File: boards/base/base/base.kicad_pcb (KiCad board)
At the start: 2 copper layers, 70.9 x 71 mm, 26 parts, among them J1 Conn_01x04_Female, J2 Conn_01x06_Female, J3 Conn_01x06_Female, J4 Screw_Terminal_01x02, J5 Conn_01x03_Female, J6 Conn_01x02_Male, Q1 BC547, Q2 BC547, Q3 2SD1047, Q4 BCP56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

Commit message: Final version of BasePCB
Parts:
- removed R6: 220, Resistor_SMD:R_0805_2012Metric
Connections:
- J5 pad 2: Net-(J5-Pad2) -> Din
- U2 pad 27: CAB_EN -> unconnected-(U2-Pad27)
- U2 pad 28: Din -> unconnected-(U2-Pad28)
- U2 pad 29: unconnected-(U2-Pad29) -> CAB_EN
- U2 pad 30: unconnected-(U2-Pad30) -> Din
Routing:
- net Din: track 5.78 -> 46.5 mm
- net Net-(J5-Pad2): track 34.7 -> 0.00 mm
- net CAB_EN: track 56.6 -> 58.0 mm
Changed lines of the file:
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@@
   (net 28 "/CAB_GROUND")
   (net 29 "Net-(Q4-Pad1)")
-  (net 30 "unconnected-(U2-Pad29)")
-  (net 31 "unconnected-(U2-Pad30)")
+  (net 30 "unconnected-(U2-Pad27)")
+  (net 31 "unconnected-(U2-Pad28)")
   (net 32 "unconnected-(U2-Pad31)")
   (net 33 "SDA")
@@
   (net 51 "CAB_RESET")
   (net 52 "Din")
-  (net 53 "Net-(J5-Pad2)")
   (footprint "TerminalBlock:TerminalBlock_Altech_AK300-2_P5.00mm" (layer "F.Cu")
     (at 115.8 93 -90)
@@
     )
   )
-  (footprint "Resistor_SMD:R_0805_2012Metric" (layer "F.Cu")
-    (at 102.7 102.9875 -90)
-    (descr "Resistor SMD 0805 (2012 Metric), square (rectangular) end terminal, IPC_7351 nominal, (Body size source: IPC-SM-782 page 72, https://www.pcb-3d.com/wordpress/wp-content/uploads/ipc-sm-782a_amendment_1_and_2.pdf), generated with kicad-footprint-generator")
-    (tags "resistor")
-    (property "Sheetfile" "base.kicad_sch")
-    (property "Sheetname" "")
-    (attr smd)
-    (fp_text reference "R6" (at 0 -1.65 90) (layer "F.SilkS")
-      (effects (font (size 1 1) (thickness 0.15)))
-    )
-    (fp_text value "220" (at 0 1.65 90) (layer "F.Fab")
-      (effects (font (size 1 1) (thickness 0.15)))
-    )
-    (fp_text user "${REFERENCE}" (at 0 0 90) (layer "F.Fab")
-      (effects (font (size 0.5 0.5) (thickness 0.08)))
-    )
-    (fp_line (start -0.227064 0.735) (end 0.227064 0.735) (layer "F.SilkS") (width 0.12))
-    (fp_line (start -0.227064 -0.735) (end 0.227064 -0.735) (layer "F.SilkS") (width 0.12))
-    (fp_line (start 1.68 0.95) (end -1.68 0.95) (layer "F.CrtYd") (width 0.05))
-    (fp_line (start -1.68 0.95) (end -1.68 -0.95) (layer "F.CrtYd") (width 0.05))
-    (fp_line (start 1.68 -0.95) (end 1.68 0.95) (layer "F.CrtYd") (width 0.05))
-    (fp_line (start -1.68 -0.95) (end 1.68 -0.95) (layer "F.CrtYd") (width 0.05))
-    (fp_line (start 1 0.625) (end -1 0.625) (layer "F.Fab") (width 0.1))
-    (fp_line (start 1 -0.625) (end 1 0.625) (layer "F.Fab") (width 0.1))
-    (fp_line (start -1 -0.625) (end 1 -0.625) (layer "F.Fab") (width 0.1))
-    (fp_line (start -1 0.625) (end -1 -0.625) (layer "F.Fab") (width 0.1))
-    (pad "1" smd roundrect (at -0.9125 0 270) (size 1.025 1.4) (layers "F.Cu" "F.Paste" "F.Mask") (roundrect_rratio 0.243902439)
-      (net 53 "Net-(J5-Pad2)") (pintype "passive"))
-    (pad "2" smd roundrect (at 0.9125 0 270) (size 1.025 1.4) (layers "F.Cu" "F.Paste" "F.Mask") (roundrect_rratio 0.243902439)
-      (net 52 "Din") (pintype "passive"))
-    (model "${KICAD6_3DMODEL_DIR}/Resistor_SMD.3dshapes/R_0805_2012Metric.wrl"
-      (offset (xyz 0 0 0))
-      (scale (xyz 1 1 1))
-      (rotate (xyz 0 0 0))
-    )
-  )
   (footprint "StackCabinet:XLE1509" (layer "F.Cu")
     (at 119.253 64.516)
@@
       (net 2 "GND") (pinfunction "Pin_1") (pintype "passive"))
     (pad "2" thru_hole oval (at 0 2.54 270) (size 1.7 1.7) (drill 1) (layers *.Cu *.Mask)
-      (net 53 "Net-(J5-Pad2)") (pinfunction "Pin_2") (pintype "passive"))
+      (net 52 "Din") (pinfunction "Pin_2") (pintype "passive"))
     (pad "3" thru_hole oval (at 0 5.08 270) (size 1.7 1.7) (drill 1) (layers *.Cu *.Mask)
       (net 3 "5V") (pinfunction "Pin_3") (pintype "passive"))
@@
     (fp_arc (start -1.91 -1.91) (mid 0 -2.701148) (end 1.91 -1.91) (layer "F.Fab") (width 0.1))
     (fp_arc (start 1.91 1.91) (mid 0 2.701148) (end -1.91 1.91) (layer "F.Fab") (width 0.1))
-    (pad "1" smd rect (at -2.75 0 180) (size 1.5 2.4) (layers "F.Cu" "F.Paste" "F.Mask")
+    (pad "1" smd rect (at -3.2 0 180) (size 2.4 2.4) (layers "F.Cu" "F.Paste" "F.Mask")
       (net 4 "Net-(D1-Pad1)") (pinfunction "1") (pintype "passive"))
-    (pad "2" smd rect (at 2.75 0 180) (size 1.5 2.4) (layers "F.Cu" "F.Paste" "F.Mask")
+    (pad "2" smd rect (at 3.2 0 180) (size 2.4 2.4) (layers "F.Cu" "F.Paste" "F.Mask")
       (net 3 "5V") (pinfunction "2") (pintype "passive"))
     (model "${KICAD6_3DMODEL_DIR}/Inductor_SMD.3dshapes/L_6.3x6.3_H3.wrl"
@@
       (net 27 "unconnected-(U2-Pad26)") (pinfunction "GPIO20/USB_D+") (pintype "bidirectional"))
     (pad "27" thru_hole oval (at 22.75 -27.94) (size 1.2 2) (drill 0.8) (layers *.Cu *.Mask)
-      (net 50 "CAB_EN") (pinfunction "GPIO21") (pintype "bidirectional"))
+      (net 30 "unconnected-(U2-Pad27)") (pinfunction "GPIO21") (pintype "bidirectional"))
     (pad "28" thru_hole oval (at 22.75 -25.4) (size 1.2 2) (drill 0.8) (layers *.Cu *.Mask)
-      (net 52 "Din") (pinfunction "GPIO47") (pintype "bidirectional"))
+      (net 31 "unconnected-(U2-Pad28)") (pinfunction "GPIO47") (pintype "bidirectional"))
     (pad "29" thru_hole oval (at 22.75 -22.86) (size 1.2 2) (drill 0.8) (layers *.Cu *.Mask)
-      (net 30 "unconnected-(U2-Pad29)") (pinfunction "GPIO48") (pintype "bidirectional"))
+      (net 50 "CAB_EN") (pinfunction "GPIO48") (pintype "bidirectional"))
     (pad "30" thru_hole oval (at 22.75 -20.32) (size 1.2 2) (drill 0.8) (layers *.Cu *.Mask)
-      (net 31 "unconnected-(U2-Pad30)") (pinfunction "GPIO45") (pintype "bidirectional"))
+      (net 52 "Din") (pinfunction "GPIO45") (pintype "bidirectional"))
     (pad "31" thru_hole oval (at 22.75 -17.78) (size 1.2 2) (drill 0.8) (layers *.Cu *.Mask)
       (net 32 "unconnected-(U2-Pad31)") (pinfunction "GPIO0") (pintype "bidirectional"))
@@
   (segment (start 88.646 58.674) (end 89.916 57.404) (width 0.5) (layer "F.Cu") (net 38))
   (segment (start 91.24 49.73) (end 101.28 49.73) (width 0.5) (layer "F.Cu") (net 38))
-  (segment (start 105.17656 106.02444) (end 105.17656 109.652) (width 0.5) (layer "F.Cu") (net 50))
-  (segment (start 131.572 103.124) (end 108.077 103.124) (width 0.5) (layer "F.Cu") (net 50))
-  (segment (start 138.176 80.518) (end 138.176 96.52) (width 0.5) (layer "F.Cu") (net 50))
-  (segment (start 108.077 103.124) (end 105.17656 106.02444) (width 0.5) (layer "F.Cu") (net 50))
-  (segment (start 138.176 96.52) (end 131.572 103.124) (width 0.5) (layer "F.Cu") (net 50))
+  (segment (start 124.0536 104.7496) (end 102.2096 104.7496) (width 0.5) (layer "F.Cu") (net 50))
+  (segment (start 138.176 90.6272) (end 124.0536 104.7496) (width 0.5) (layer "F.Cu") (net 50))
+  (segment (start 100.25656 106.70264) (end 100.25656 110.05) (width 0.5) (layer "F.Cu") (net 50))
+  (segment (start 102.2096 104.7496) (end 100.25656 106.70264) (width 0.5) (layer "F.Cu") (net 50))
+  (segment (start 138.176 80.518) (end 138.176 90.6272) (width 0.5) (layer "F.Cu") (net 50))
   (segment (start 85.598 76.708) (end 85.598 80.2405) (width 0.5) (layer "F.Cu") (net 51))
-  (segment (start 102.7 103.9) (end 102.63656 103.96344) (width 0.5) (layer "F.Cu") (net 52))
-  (segment (start 102.63656 103.96344) (end 102.63656 109.652) (width 0.5) (layer "F.Cu") (net 52))
-  (segment (start 129.667 93.133) (end 126.7 96.1) (width 0.5) (layer "F.Cu") (net 53))
-  (segment (start 126.7 96.1) (end 105.7 96.1) (width 0.5) (layer "F.Cu") (net 53))
-  (segment (start 105.7 96.1) (end 102.7 99.1) (width 0.5) (layer "F.Cu") (net 53))
-  (segment (start 129.667 90.805) (end 129.667 93.133) (width 0.5) (layer "F.Cu") (net 53))
-  (segment (start 102.7 99.1) (end 102.7 102.075) (width 0.5) (layer "F.Cu") (net 53))
+  (segment (start 103.9876 96.0628) (end 97.71656 102.33384) (width 0.5) (layer "F.Cu") (net 52))
+  (segment (start 129.667 94.234) (end 127.8382 96.0628) (width 0.5) (layer "F.Cu") (net 52))
+  (segment (start 129.667 90.805) (end 129.667 94.234) (width 0.5) (layer "F.Cu") (net 52))
+  (segment (start 127.8382 96.0628) (end 103.9876 96.0628) (width 0.5) (layer "F.Cu") (net 52))
+  (segment (start 97.71656 102.33384) (end 97.71656 110.05) (width 0.5) (layer "F.Cu") (net 52))
   (zone (net 2) (net_name "GND") (layer "F.Cu") (hatch edge 0.508)
     (connect_pads (clearance 0.508))

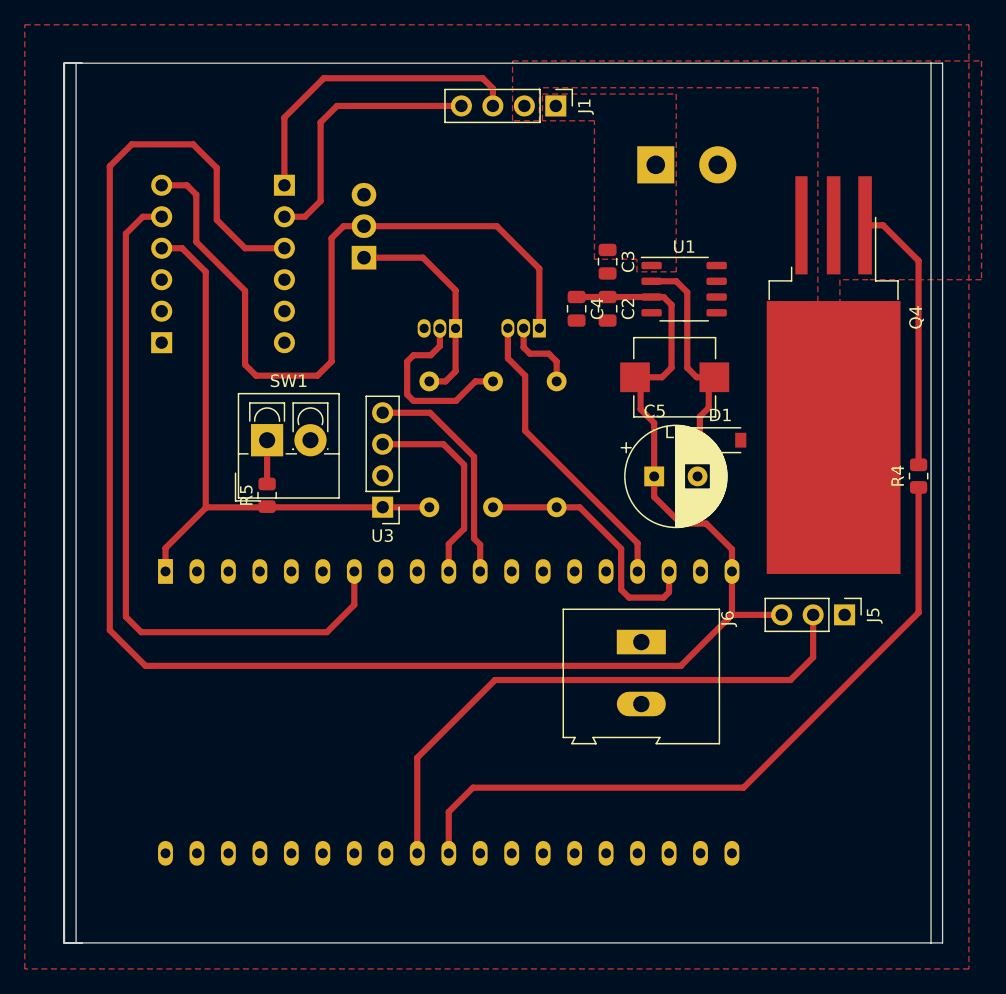
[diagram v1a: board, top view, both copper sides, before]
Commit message: Added diode on base
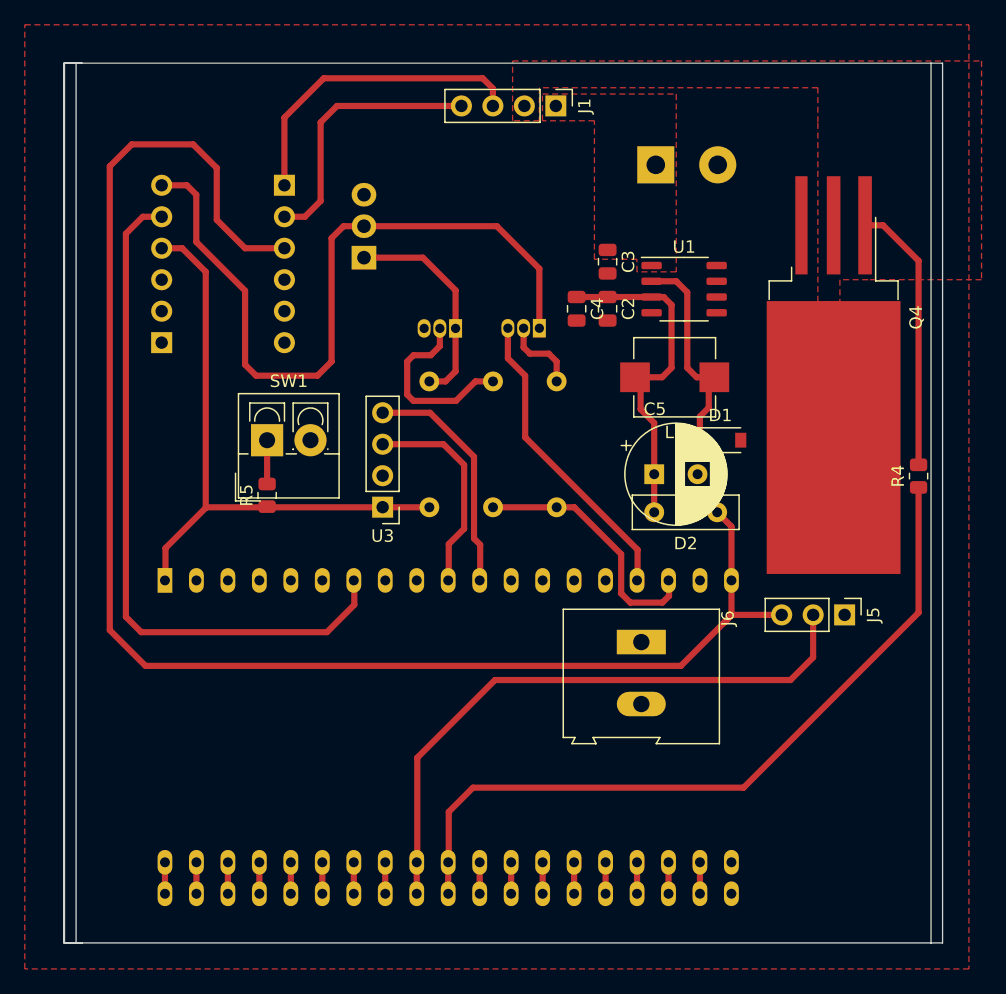
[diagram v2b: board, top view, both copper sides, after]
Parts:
- added D2: D, Resistor_THT:R_Box_L8.4mm_W2.5mm_P5.08mm, F.Cu at (121.9, 82.5)
- moved U2 0.72 mm to (77.4, 88.0)
- moved C5 0.18 mm to (116.8, 79.5)
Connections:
- C2 pad 1: 5V -> VOUT
- C4 pad 1: 5V -> VOUT
- C5 pad 1: 5V -> VOUT
- L1 pad 2: 5V -> VOUT
- U1 pad 3: 5V -> VOUT
- U2 pad 18: GND -> unconnected-(U2-Pad18)
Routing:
- net 5V: track 155.4 -> 125.0 mm
- net VOUT: track 0.00 -> 27.2 mm
- net GND: track 0.00 -> 5.08 mm
- net unconnected-(U2-Pad21): track 0.00 -> 2.54 mm
- net unconnected-(U2-Pad37): track 0.00 -> 2.54 mm
- net unconnected-(U2-Pad36): track 0.00 -> 2.54 mm
- net unconnected-(U2-Pad35): track 0.00 -> 2.54 mm
- net unconnected-(U2-Pad34): track 0.00 -> 2.54 mm
- net unconnected-(U2-Pad33): track 0.00 -> 2.54 mm
- net unconnected-(U2-Pad31): track 0.00 -> 2.54 mm
- net unconnected-(U2-Pad28): track 0.00 -> 2.54 mm
- net unconnected-(U2-Pad27): track 0.00 -> 2.54 mm
- net unconnected-(U2-Pad26): track 0.00 -> 2.54 mm
- net unconnected-(U2-Pad25): track 0.00 -> 2.54 mm
- net unconnected-(U2-Pad24): track 0.00 -> 2.54 mm
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
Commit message: Backups
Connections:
- net /CAB_GROUND renamed CAB_GROUND
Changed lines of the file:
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@@
   (net 26 "unconnected-(U2-Pad25)")
   (net 27 "unconnected-(U2-Pad26)")
-  (net 28 "/CAB_GROUND")
+  (net 28 "CAB_GROUND")
   (net 29 "Net-(Q4-Pad1)")
   (net 30 "unconnected-(U2-Pad27)")
@@
       (net 1 "VBUS") (pinfunction "Pin_1") (pintype "passive"))
     (pad "2" thru_hole oval (at 0 2.54 270) (size 1.7 1.7) (drill 1) (layers *.Cu *.Mask)
-      (net 28 "/CAB_GROUND") (pinfunction "Pin_2") (pintype "passive"))
+      (net 28 "CAB_GROUND") (pinfunction "Pin_2") (pintype "passive"))
     (pad "3" thru_hole oval (at 0 5.08 270) (size 1.7 1.7) (drill 1) (layers *.Cu *.Mask)
       (net 37 "GDA_H") (pinfunction "Pin_3") (pintype "passive"))
@@
       (net 29 "Net-(Q4-Pad1)") (pinfunction "B") (pintype "input"))
     (pad "2" smd rect (at -7.4375 0 270) (size 7.925 1.1) (layers "F.Cu" "F.Paste" "F.Mask")
-      (net 28 "/CAB_GROUND") (pinfunction "C") (pintype "passive"))
+      (net 28 "CAB_GROUND") (pinfunction "C") (pintype "passive"))
     (pad "2" smd rect (at 9.6875 0 270) (size 22.025 10.8) (layers "F.Cu" "F.Mask")
-      (net 28 "/CAB_GROUND") (pinfunction "C") (pintype "passive"))
+      (net 28 "CAB_GROUND") (pinfunction "C") (pintype "passive"))
     (pad "3" smd rect (at -7.4375 2.595 270) (size 7.925 0.99) (layers "F.Cu" "F.Paste" "F.Mask")
       (net 2 "GND") (pinfunction "E") (pintype "passive"))
@@
     )
   )
-  (zone (net 28) (net_name "/CAB_GROUND") (layer "F.Cu") (hatch edge 0.508)
+  (zone (net 28) (net_name "CAB_GROUND") (layer "F.Cu") (hatch edge 0.508)
     (priority 1)
     (connect_pads yes (clearance 0.508))

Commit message: Base V2
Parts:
- removed D2: D, Resistor_THT:R_Box_L8.4mm_W2.5mm_P5.08mm
- removed Q2: BC547, Package_TO_SOT_THT:TO-92_Inline
- removed Q3: 2SD1047, Package_TO_SOT_THT:TO-220-3_Vertical
- removed Q4: BCP56, Package_TO_SOT_SMD:TO-263-3_TabPin2
- removed R1, R2: 1k, Resistor_THT:R_Axial_DIN0207_L6.3mm_D2.5mm_P10.16mm_Horizontal
- removed R3: 10k, Resistor_THT:R_Axial_DIN0207_L6.3mm_D2.5mm_P10.16mm_Horizontal
- removed R5: 10k, Resistor_SMD:R_0805_2012Metric
- added D3: D, Resistor_THT:R_Box_L8.4mm_W2.5mm_P5.08mm, F.Cu at (98.9, 69.2)
- added J7: Conn_01x02_Female, TerminalBlock_Altech:Altech_AK300_1x02_P5.00mm_45-Degree, B.Cu at (128.5, 51.2)
- added J8: Conn_01x03_Female, Connector_PinHeader_2.54mm:PinHeader_1x03_P2.54mm_Vertical, F.Cu at (127.8, 99.6)
- added R6: 100, Resistor_THT:R_Axial_DIN0207_L6.3mm_D2.5mm_P5.08mm_Vertical, F.Cu at (102.7, 83.7)
- added R7: 100, Resistor_THT:R_Axial_DIN0207_L6.3mm_D2.5mm_P5.08mm_Vertical, F.Cu at (95.9, 49.8)
- added R8: 100, Resistor_THT:R_Axial_DIN0207_L6.3mm_D2.5mm_P5.08mm_Vertical, F.Cu at (95.9, 54.5)
- Q1: moved to F.Cu
- R4: value 1k -> 10k; footprint Resistor_SMD:R_0805_2012Metric -> Resistor_THT:R_Axial_DIN0207_L6.3mm_D2.5mm_P5.08mm_Vertical
- SW1: footprint TerminalBlock_4Ucon:TerminalBlock_4Ucon_1x02_P3.50mm_Vertical -> Connector_PinHeader_2.54mm:PinHeader_1x02_P2.54mm_Vertical
- moved R4 35.7 mm to (104.0, 69.2), turned to -90 degrees
- moved SW1 30.9 mm to (79.9, 107.1), turned to -90 degrees
- moved Q1 11.8 mm to (105.3, 78.6)
- moved J5 2.79 mm to (132.2, 93.6)
- moved C5 1.65 mm to (115.2, 79.5)
- moved D1 0.74 mm to (121.5, 77.1)
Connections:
- C2 pad 1: VOUT -> 5V
- C4 pad 1: VOUT -> 5V
- C5 pad 1: VOUT -> 5V
- J2 pad 1: GDA_H -> Net-(J2-Pad1)
- J2 pad 2: SEL0 -> Net-(J2-Pad2)
- J2 pad 4: unconnected-(J2-Pad4) -> GND
- J3 pad 3: unconnected-(J3-Pad3) -> GND
- L1 pad 2: VOUT -> 5V
- Q1 pad 3: GND -> GDA_L
- R4 pad 1: CAB_EN -> Tx
- R4 pad 2: Net-(Q4-Pad1) -> Net-(Q1-Pad2)
- U1 pad 3: VOUT -> 5V
- U2 pad 13: unconnected-(U2-Pad13) -> Rx
- U2 pad 15: unconnected-(U2-Pad15) -> Tx
- U2 pad 16: Rx -> unconnected-(U2-Pad16)
- U2 pad 17: Tx -> unconnected-(U2-Pad17)
- U2 pad 37: unconnected-(U2-Pad37) -> CAB_RESET
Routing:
- net 5V: track 125.0 -> 187.9 mm
- net VOUT: track 27.2 -> 0.00 mm
- net CAB_EN: track 60.6 -> 34.2 mm
- net Net-(Q4-Pad1): track 22.0 -> 0.00 mm
- net Rx: track 24.0 -> 4.35 mm
- net GDA_H: track 25.4 -> 10.5 mm
- net GDA_L: track 59.6 -> 44.9 mm
- net SEL0: track 21.7 -> 8.52 mm
- net Net-(Q1-Pad2): track 15.0 -> 4.45 mm
- net Net-(Q1-Pad1): track 17.5 -> 6.99 mm
- net Net-(J2-Pad1): track 0.00 -> 8.78 mm
- net Net-(J2-Pad2): track 0.00 -> 7.57 mm
- net Tx: track 21.5 -> 28.8 mm
- net Net-(Q2-Pad2): track 6.29 -> 0.00 mm
- net 3V3: track 48.0 -> 44.2 mm
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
